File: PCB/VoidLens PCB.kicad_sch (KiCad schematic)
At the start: 79 parts, among them IC1 BMI270, J1 solder pad, J2 JST-XH-2 Pin, J4 JST_XH for led Strip, J5 Programming_Pins, SW1 K3-1391A, SW2 SW_Push_DPDT, SW5 K2-1157SP-I4SW-04, U1 BQ24074RGT, U2 ATmega32U4-M, U3 NRF24L01, U5 TPS61022, U6 TPS27081ADDCR, U7 TPS27081ADDCR, Y1 16Mhz, Y2 16mhz

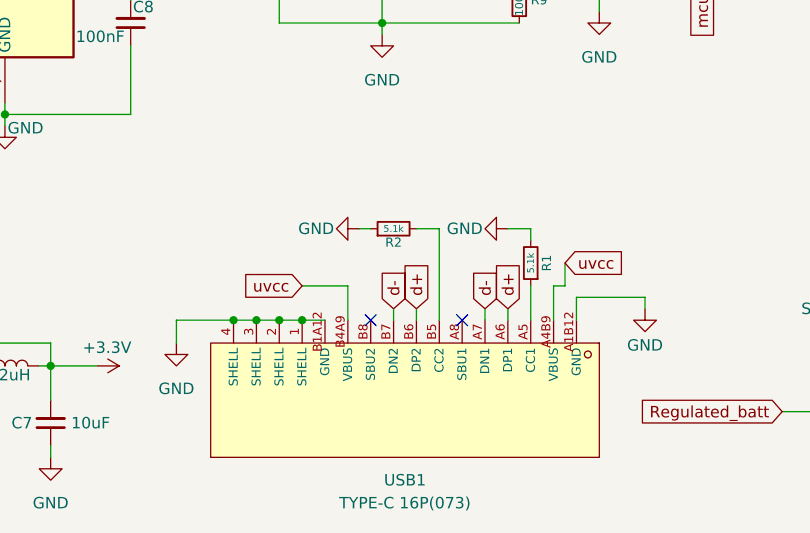
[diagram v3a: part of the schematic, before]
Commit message: finihed routing
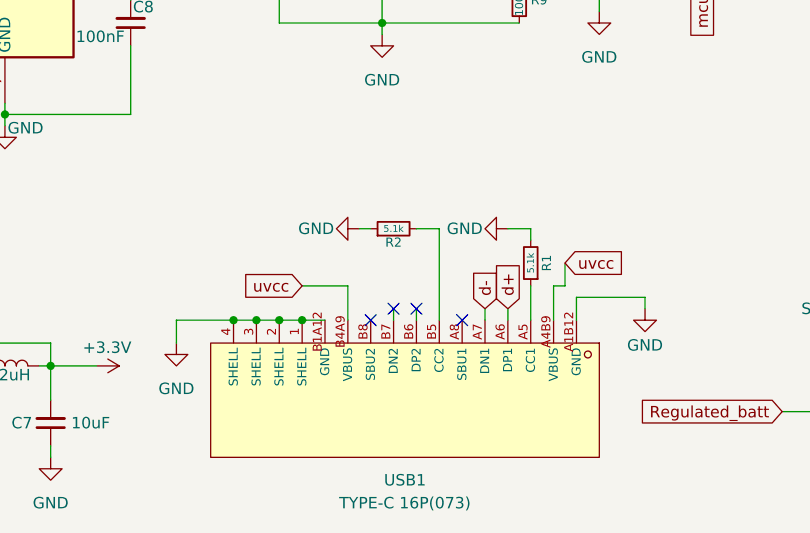
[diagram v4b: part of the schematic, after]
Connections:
- net d+: no longer USB1.B6 (DP2)
- net d-: no longer USB1.B7 (DN2)
- no-connect marks 25 -> 27
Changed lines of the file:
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@@
 	)
 	(no_connect
+		(at 102.87 170.18)
+	)
+	(no_connect
 		(at 72.39 124.46)
 	)
@@
 	)
 	(no_connect
+		(at 105.41 170.18)
+	)
+	(no_connect
 		(at 41.91 127)
 	)
@@
 		)
 	)
+	(global_label "d-"
+		(shape input)
+		(at 113.03 170.18 90)
+		(fields_autoplaced yes)
+		(effects
+			(font
+				(size 1.27 1.27)
+			)
+			(justify left)
+		)
+		(property "Intersheetrefs" "${INTERSHEET_REFS}"
+			(at 113.03 164.4734 90)
+			(hide yes)
+			(show_name no)
+			(do_not_autoplace no)
+			(effects
+				(font
+					(size 1.27 1.27)
+				)
+				(justify left)
+			)
+		)
+	)
 	(global_label "batt_main"
 		(shape input)
@@
 		)
 	)
-	(global_label "d-"
-		(shape input)
-		(at 102.87 170.18 90)
-		(fields_autoplaced yes)
-		(effects
-			(font
-				(size 1.27 1.27)
-			)
-			(justify left)
-		)
-		(property "Intersheetrefs" "${INTERSHEET_REFS}"
-			(at 102.87 164.4734 90)
-			(hide yes)
-			(show_name no)
-			(do_not_autoplace no)
-			(effects
-				(font
-					(size 1.27 1.27)
-				)
-				(justify left)
-			)
-		)
-	)
-	(global_label "d-"
-		(shape input)
-		(at 113.03 170.18 90)
-		(fields_autoplaced yes)
-		(effects
-			(font
-				(size 1.27 1.27)
-			)
-			(justify left)
-		)
-		(property "Intersheetrefs" "${INTERSHEET_REFS}"
-			(at 113.03 164.4734 90)
-			(hide yes)
-			(show_name no)
-			(do_not_autoplace no)
-			(effects
-				(font
-					(size 1.27 1.27)
-				)
-				(justify left)
-			)
-		)
-	)
 	(global_label "Regulated_batt"
 		(shape input)
@@
 			(hide yes)
 			(show_name no)
-			(do_not_autoplace no)
-			(effects
-				(font
-					(size 1.27 1.27)
-				)
-				(justify left)
-			)
-		)
-	)
-	(global_label "d+"
-		(shape input)
-		(at 105.41 170.18 90)
-		(fields_autoplaced yes)
-		(effects
-			(font
-				(size 1.27 1.27)
-			)
-			(justify left)
-		)
-		(property "Intersheetrefs" "${INTERSHEET_REFS}"
-			(at 105.41 164.4734 90)
-			(hide yes)
-			(show_name no)
